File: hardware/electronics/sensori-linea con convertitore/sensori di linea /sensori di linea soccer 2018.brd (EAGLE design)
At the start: 88.1 x 42 mm, 27 parts, among them T1 BP103, T2 BP103, T3 BP103, T4 BP103

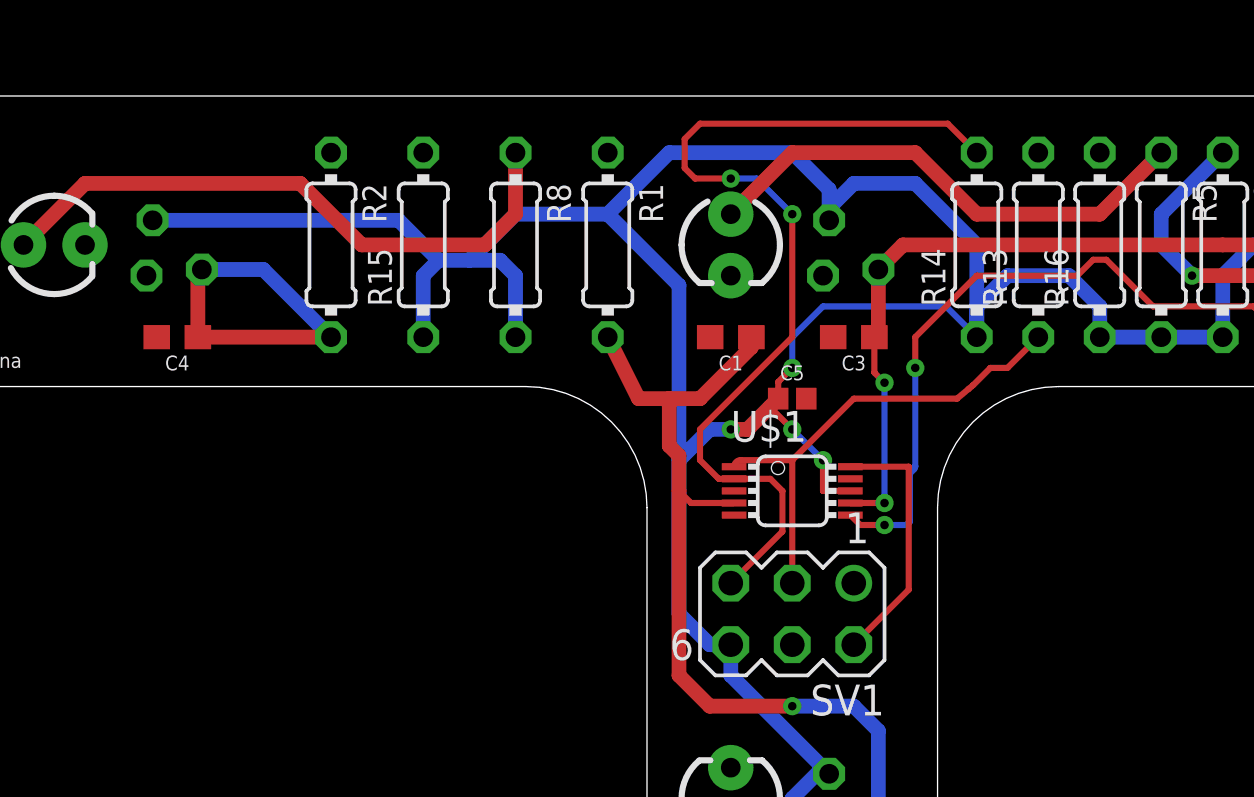
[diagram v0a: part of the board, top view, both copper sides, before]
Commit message: aggiunta fie sensori di linea nuovi
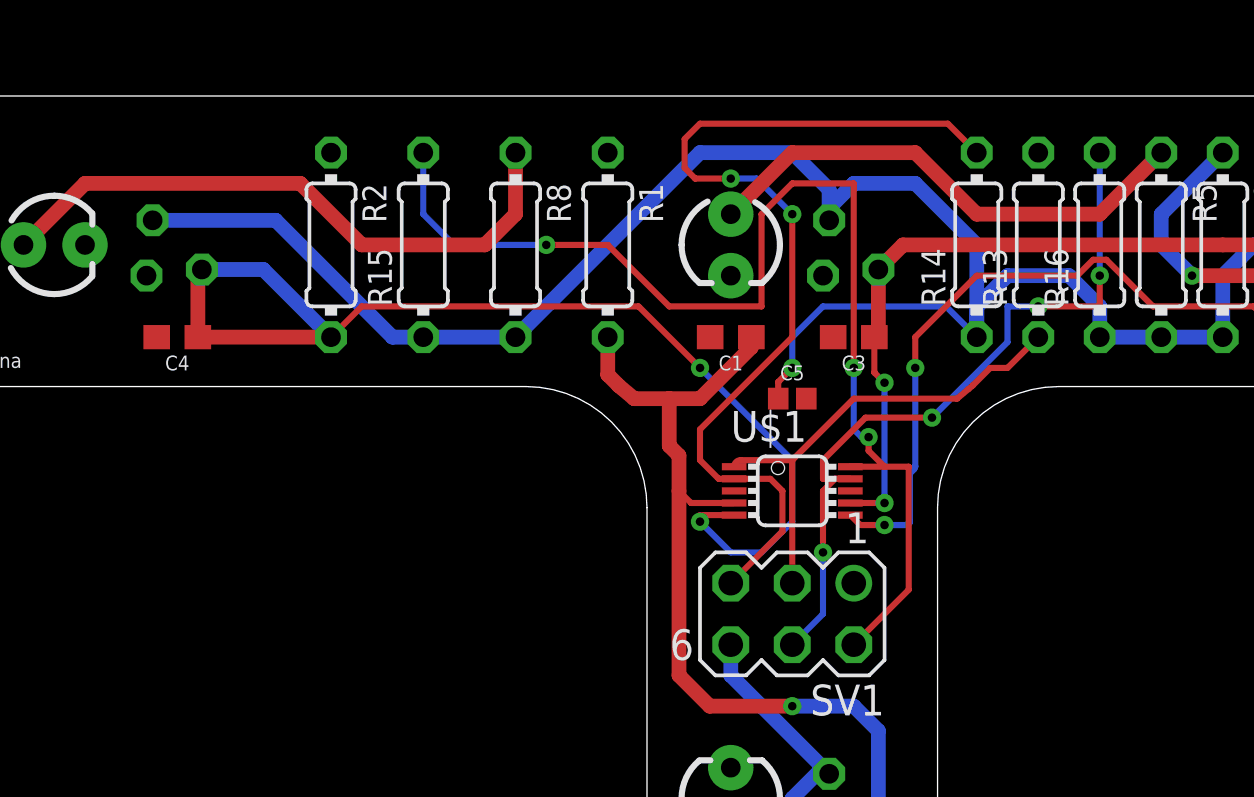
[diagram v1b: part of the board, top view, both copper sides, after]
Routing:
- net SCL: track 10.7 -> 49.3 mm, vias 0 -> 3
- net VCC: track 145.6 -> 108.6 mm, vias 4 -> 1
- net SDA: track 0.00 -> 31.4 mm, vias 0 -> 4
- net OUT2: track 14.9 -> 46.1 mm, vias 0 -> 2

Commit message: sensori di linea 2018
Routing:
- net VCC: track 108.6 -> 128.6 mm, vias 1 -> 3
- net SDA: track 31.4 -> 38.1 mm, vias 4 -> 5
- net ALERT: track 39.6 -> 35.7 mm
- net GND: track 0.00 -> 3.18 mm, vias 1 -> 4
- net OUT2: track 46.1 -> 43.0 mm
- net OUT3: track 42.7 -> 44.9 mm

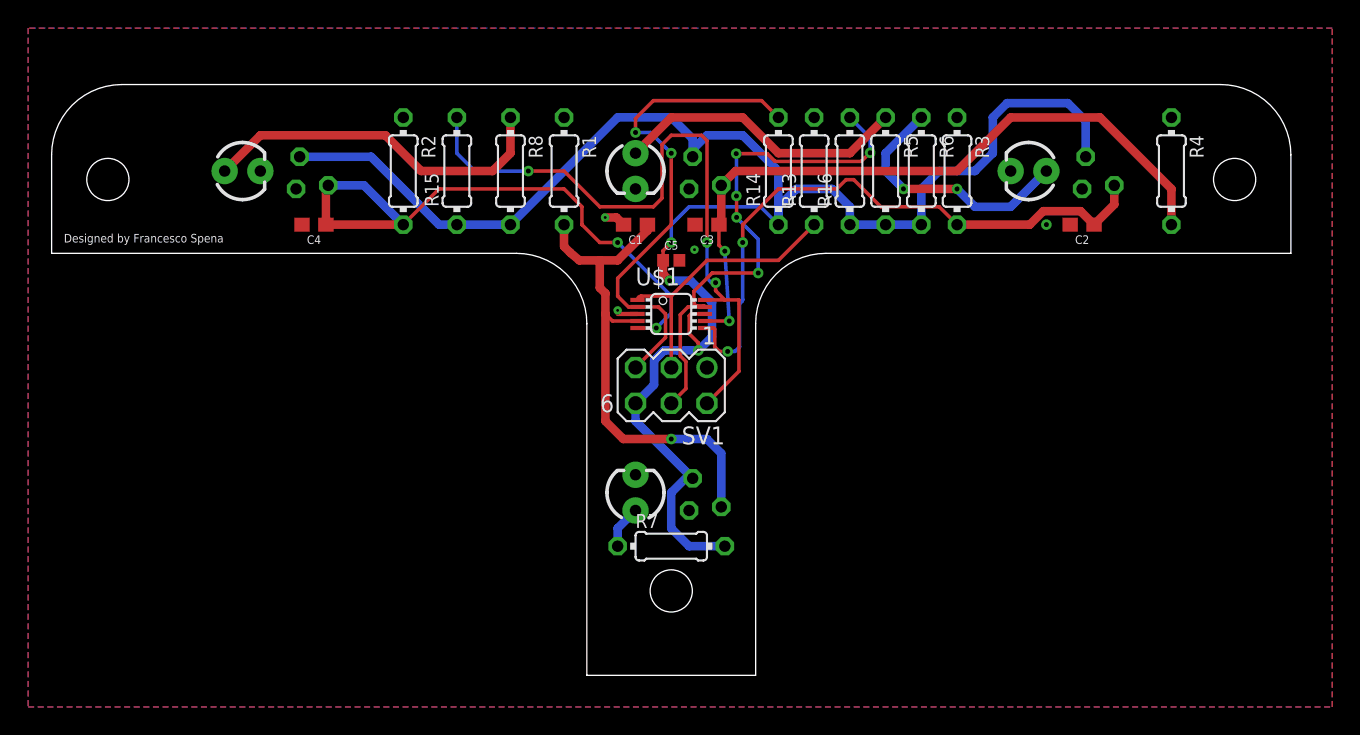
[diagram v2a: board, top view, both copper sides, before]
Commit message: sensori di linea completi 2018
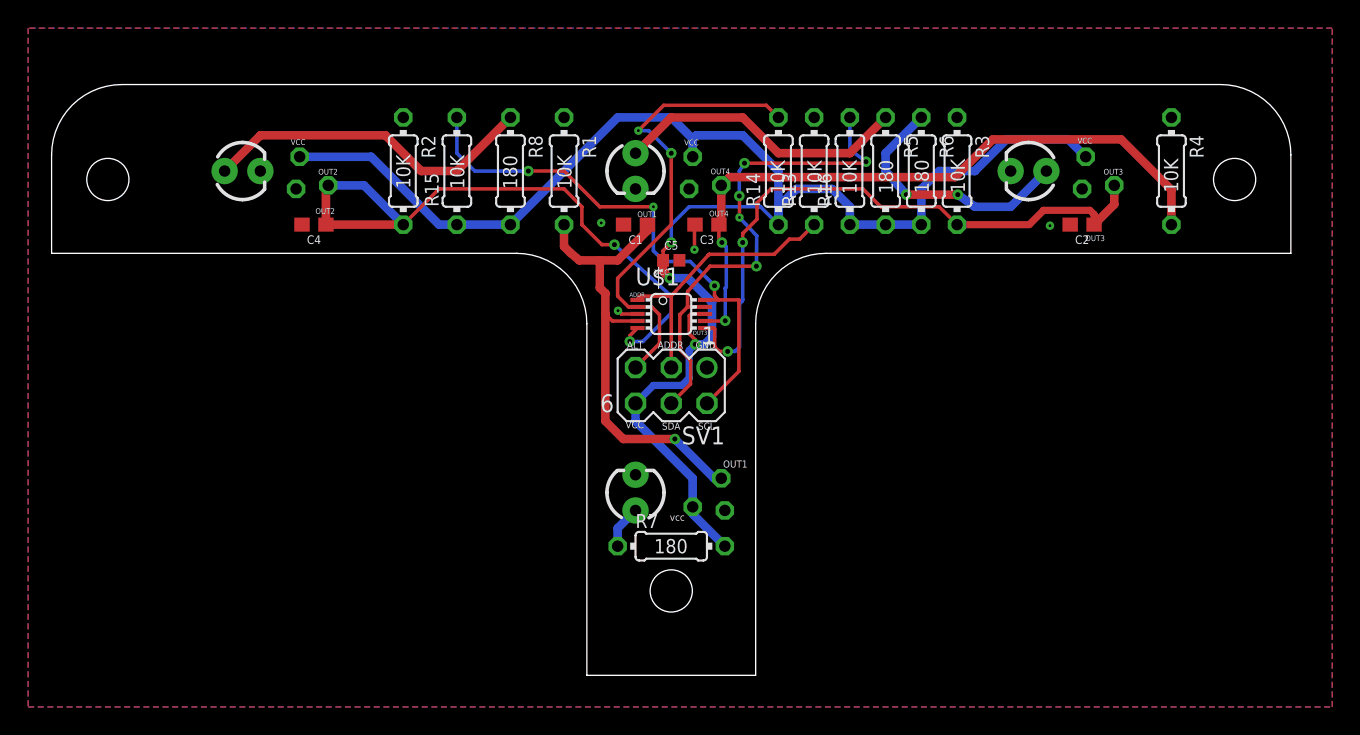
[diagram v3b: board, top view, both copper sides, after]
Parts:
- R1, R13, R14, R15, R16, R2, R3, R4: value (none) -> 10K
- R5, R6, R7: value (none) -> 180
- turned T1 to 270 degrees
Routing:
- net SCL: track 49.1 -> 39.2 mm
- net VCC: track 128.6 -> 119.8 mm
- net OUT1: track 36.2 -> 33.2 mm
- net ALERT: track 35.7 -> 33.8 mm
- net OUT2: track 43.0 -> 44.9 mm
- net SDA: track 38.1 -> 36.3 mm
- net OUT4: track 50.5 -> 48.7 mm
- net N$5: track 25.5 -> 24.0 mm
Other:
- board text added: "10K"
- board text added: "180"
- board text added: "ADDR"
- board text added: "ALT"
- board text added: "GND"
- board text added: "OUT1"
- board text added: "OUT2"
- board text added: "OUT3"
- board text added: "OUT4"
- board text added: "SCL"
- board text added: "SDA"
- board text added: "VCC"
- board text added: "vcc"
